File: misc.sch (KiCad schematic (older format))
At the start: 40 parts, among them J13 MICROSD_SLOT_TFP09-2-12B, P13 EXT_SD, P14 LCD, P15 LIMIT_SWITCHES, P16 LIMIT_SWITCHES_V, P17 CONN_01X03, P18 CONN_01X03, P19 CONN_01X03, P20 CONN_01X03, P21 THERMISTORS, P22 CONN_01X05, P25 CONN_01X03, SW1 RESET, U2 24LC256, U3 ESP-12E

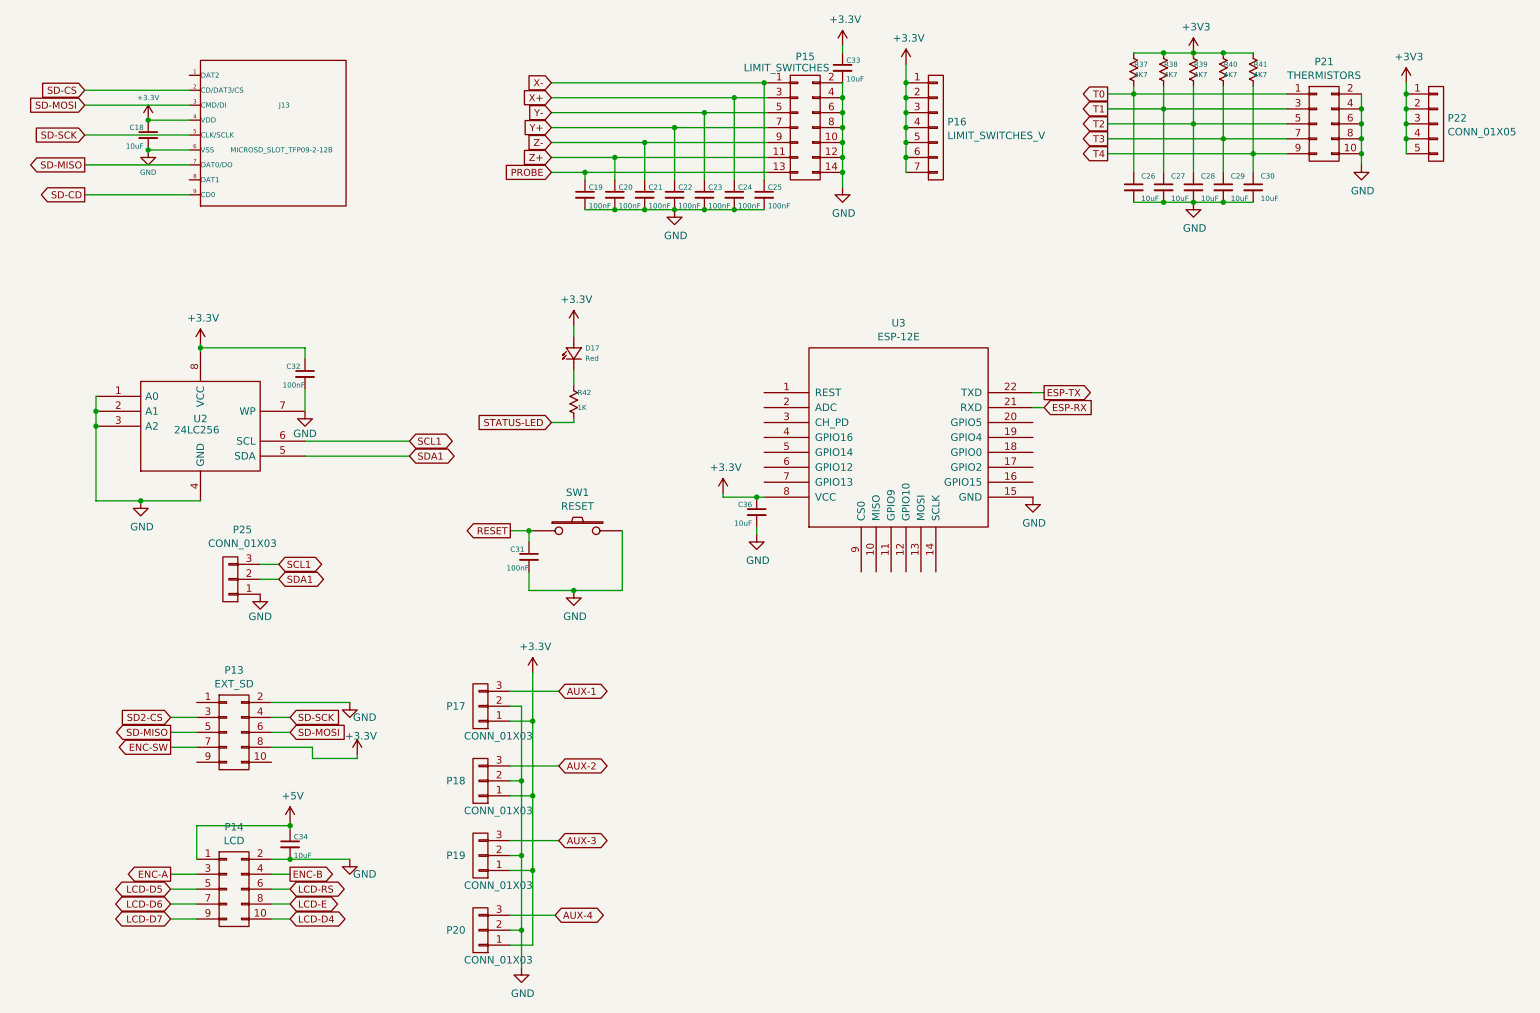
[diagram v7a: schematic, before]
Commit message: Added minimal arduino mega support
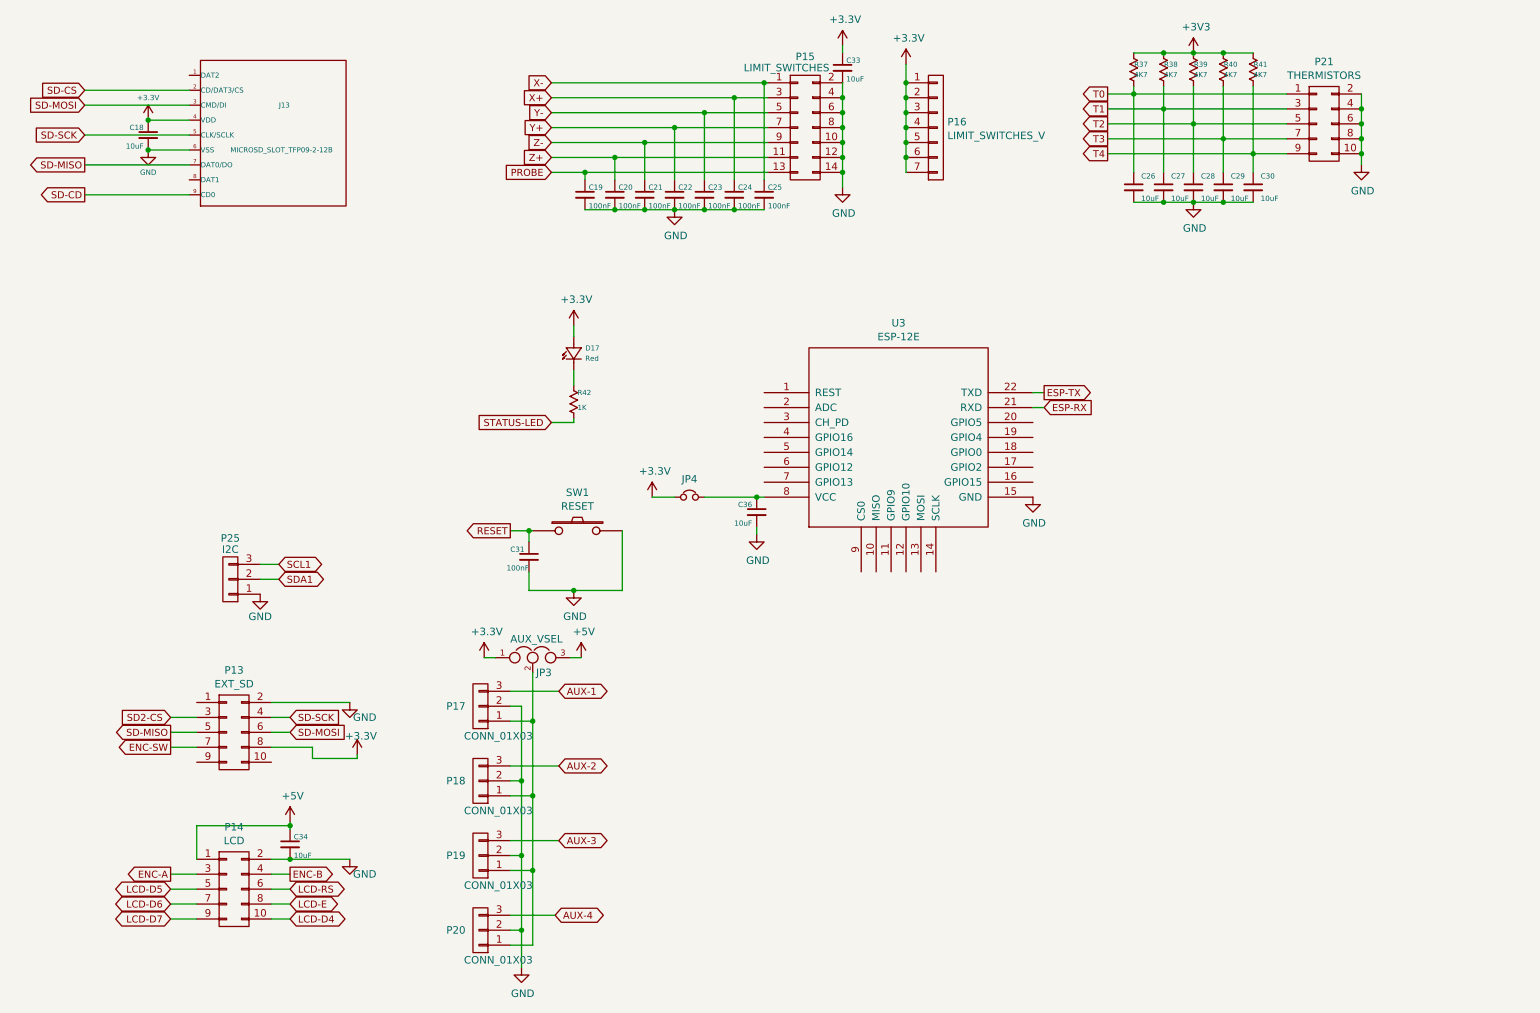
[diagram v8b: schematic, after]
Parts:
- removed C32: 100nF, capacitors:C_0603, symbol C_Small
- removed P22: CONN_01X05, headers:CON_HDR_1x5_2.54mm, symbol CONN_01X05
- removed U2: 24LC256, soic:SOIC8, symbol 24C16
- added JP3: AUX_VSEL, headers:CON_HDR_1x3_2.54mm, symbol JUMPER3
- added JP4: Jumper_NC_Small, headers:CON_HDR_1x2_2.54mm, symbol Jumper_NC_Small
- P25: value CONN_01X03 -> I2C
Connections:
- net +3V3: now also JP3.1, JP4.1; no longer C36.1, P17.1 (P1), P18.1 (P1), P19.1 (P1), P20.1 (P1), U3.8 (VCC)
- net +5V: now also JP3.3
- new net: JP3.2, P17.1 (P1), P18.1 (P1), P19.1 (P1), P20.1 (P1)
- new net: C36.1, JP4.2, U3.8 (VCC)
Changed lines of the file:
@@
 $EndComp
 $Comp
-L GND #PWR88
+L GND #PWR87
 U 1 1 568D834C
 P 9950 2075
-F 0 "#PWR88" H 9950 1825 50  0001 C CNN
+F 0 "#PWR87" H 9950 1825 50  0001 C CNN
 F 1 "GND" H 9958 1901 50  0000 C CNN
 F 2 "" H 9950 2075 50  0000 C CNN
@@
 $EndComp
 $Comp
-L GND #PWR87
+L GND #PWR86
 U 1 1 568D94E5
 P 8825 2325
-F 0 "#PWR87" H 8825 2075 50  0001 C CNN
+F 0 "#PWR86" H 8825 2075 50  0001 C CNN
 F 1 "GND" H 8833 2151 50  0000 C CNN
 F 2 "" H 8825 2325 50  0000 C CNN
@@
 $EndComp
 $Comp
-L +3V3 #PWR86
+L +3V3 #PWR85
 U 1 1 568D9512
 P 8825 1325
-F 0 "#PWR86" H 8825 1175 50  0001 C CNN
+F 0 "#PWR85" H 8825 1175 50  0001 C CNN
 F 1 "+3V3" H 8843 1499 50  0000 C CNN
 F 2 "" H 8825 1325 50  0000 C CNN
 F 3 "" H 8825 1325 50  0000 C CNN
 	1    8825 1325
-	1    0    0    -1
-$EndComp
-$Comp
-L CONN_01X05 P22
-U 1 1 568D989A
-P 10450 1800
-F 0 "P22" H 10527 1838 50  0000 L CNN
-F 1 "CONN_01X05" H 10527 1746 50  0000 L CNN
-F 2 "headers:CON_HDR_1x5_2.54mm" H 10450 1800 50  0001 C CNN
-F 3 "" H 10450 1800 50  0000 C CNN
-	1    10450 1800
-	1    0    0    -1
-$EndComp
-$Comp
-L +3V3 #PWR89
-U 1 1 568D9A56
-P 10250 1525
-F 0 "#PWR89" H 10250 1375 50  0001 C CNN
-F 1 "+3V3" H 10268 1699 50  0000 C CNN
-F 2 "" H 10250 1525 50  0000 C CNN
-F 3 "" H 10250 1525 50  0000 C CNN
-	1    10250 1525
-	1    0    0    -1
-$EndComp
-$Comp
-L 24C16 U2
-U 1 1 568DA07F
-P 2175 3825
-F 0 "U2" H 2175 3875 50  0000 C CNN
-F 1 "24LC256" H 2150 3800 50  0000 C CNN
-F 2 "soic:SOIC8" H 2175 3825 50  0001 C CNN
-F 3 "" H 2175 3825 50  0000 C CNN
-	1    2175 3825
-	1    0    0    -1
-$EndComp
-$Comp
-L GND #PWR71
-U 1 1 568DA443
-P 2875 3725
-F 0 "#PWR71" H 2875 3475 50  0001 C CNN
-F 1 "GND" H 2875 3575 50  0000 C CNN
-F 2 "" H 2875 3725 50  0000 C CNN
-F 3 "" H 2875 3725 50  0000 C CNN
-	1    2875 3725
-	1    0    0    -1
-$EndComp
-$Comp
-L GND #PWR65
-U 1 1 568DA52A
-P 1775 4325
-F 0 "#PWR65" H 1775 4075 50  0001 C CNN
-F 1 "GND" H 1783 4151 50  0000 C CNN
-F 2 "" H 1775 4325 50  0000 C CNN
-F 3 "" H 1775 4325 50  0000 C CNN
-	1    1775 4325
-	1    0    0    -1
-$EndComp
-$Comp
-L +3.3V #PWR68
-U 1 1 568DA65A
-P 2175 3275
-F 0 "#PWR68" H 2175 3125 50  0001 C CNN
-F 1 "+3.3V" H 2193 3449 50  0000 C CNN
-F 2 "" H 2175 3275 50  0000 C CNN
-F 3 "" H 2175 3275 50  0000 C CNN
-	1    2175 3275
 	1    0    0    -1
 $EndComp
@@
 $EndComp
 $Comp
-L GND #PWR83
+L GND #PWR82
 U 1 1 568D90A7
 P 6475 2225
-F 0 "#PWR83" H 6475 1975 50  0001 C CNN
+F 0 "#PWR82" H 6475 1975 50  0001 C CNN
 F 1 "GND" H 6483 2051 50  0000 C CNN
 F 2 "" H 6475 2225 50  0000 C CNN
@@
 $EndComp
 $Comp
-L +3.3V #PWR84
+L +3.3V #PWR83
 U 1 1 568D9133
 P 6900 1400
-F 0 "#PWR84" H 6900 1250 50  0001 C CNN
+F 0 "#PWR83" H 6900 1250 50  0001 C CNN
 F 1 "+3.3V" H 6918 1574 50  0000 C CNN
 F 2 "" H 6900 1400 50  0000 C CNN
@@
 	1    0    0    -1
 $EndComp
-Text GLabel 3575 3925 2    47   BiDi ~ 0
-SCL1
-Text GLabel 3575 4025 2    47   BiDi ~ 0
-SDA1
 $Comp
 L CONN_01X03 P20
@@
 	8250 2000 9450 2000
 Connection ~ 9225 2000
-Wire Wire Line
-	10250 1525 10250 2000
-Connection ~ 10250 1600
-Connection ~ 10250 1700
-Connection ~ 10250 1800
-Connection ~ 10250 1900
-Wire Wire Line
-	1475 3625 1475 4325
-Wire Wire Line
-	1475 4325 2175 4325
-Connection ~ 1475 3725
-Connection ~ 1475 3825
-Connection ~ 1775 4325
-Wire Wire Line
-	2175 3275 2175 3325
 Wire Wire Line
 	6900 1400 6900 2125
@@
 Connection ~ 5550 2375
 Connection ~ 5750 2375
-Wire Wire Line
-	2875 3925 3575 3925
-Wire Wire Line
-	2875 4025 3575 4025
 $Comp
 L CONN_01X03 P19
@@
 	4325 7200 4250 7200
 $Comp
-L GND #PWR75
+L GND #PWR74
 U 1 1 568EABC9
 P 4325 7450
-F 0 "#PWR75" H 4325 7200 50  0001 C CNN
+F 0 "#PWR74" H 4325 7200 50  0001 C CNN
 F 1 "GND" H 4333 7276 50  0000 C CNN
 F 2 "" H 4325 7450 50  0000 C CNN
@@
 $EndComp
 $Comp
-L +3.3V #PWR76
+L +3.3V #PWR73
 U 1 1 568EAEBC
-P 4400 5475
-F 0 "#PWR76" H 4400 5325 50  0001 C CNN
-F 1 "+3.3V" H 4418 5649 50  0000 C CNN
-F 2 "" H 4400 5475 50  0000 C CNN
-F 3 "" H 4400 5475 50  0000 C CNN
-	1    4400 5475
+P 4075 5375
+F 0 "#PWR73" H 4075 5225 50  0001 C CNN
+F 1 "+3.3V" H 4093 5549 50  0000 C CNN
+F 2 "" H 4075 5375 50  0000 C CNN
+F 3 "" H 4075 5375 50  0000 C CNN
+	1    4075 5375
 	1    0    0    -1
 $EndComp
@@
 SD-SCK
 $Comp
-L GND #PWR72
+L GND #PWR70
 U 1 1 568F027E
 P 3175 5675
-F 0 "#PWR72" H 3175 5425 50  0001 C CNN
+F 0 "#PWR70" H 3175 5425 50  0001 C CNN
 F 1 "GND" H 3275 5575 50  0000 C CNN
 F 2 "" H 3175 5675 50  0000 C CNN
@@
 	2650 5675 3175 5675
 $Comp
-L +3.3V #PWR74
+L +3.3V #PWR72
 U 1 1 568F1103
 P 3225 6025
-F 0 "#PWR74" H 3225 5875 50  0001 C CNN
+F 0 "#PWR72" H 3225 5875 50  0001 C CNN
 F 1 "+3.3V" H 3250 6150 50  0000 C CNN
 F 2 "" H 3225 6025 50  0000 C CNN
@@
 	3225 6050 3225 6025
 $Comp
-L +5V #PWR70
+L +5V #PWR69
 U 1 1 568F17B3
 P 2775 6475
-F 0 "#PWR70" H 2775 6325 50  0001 C CNN
+F 0 "#PWR69" H 2775 6325 50  0001 C CNN
 F 1 "+5V" H 2793 6649 50  0000 C CNN
 F 2 "" H 2775 6475 50  0000 C CNN
@@
 $EndComp
 $Comp
-L GND #PWR73
+L GND #PWR71
 U 1 1 568F18BA
 P 3175 6725
-F 0 "#PWR73" H 3175 6475 50  0001 C CNN
+F 0 "#PWR71" H 3175 6475 50  0001 C CNN
 F 1 "GND" H 3275 6625 50  0000 C CNN
 F 2 "" H 3175 6725 50  0000 C CNN
@@
 	4675 3800 4675 3775
 $Comp
-L +3.3V #PWR77
+L +3.3V #PWR75
 U 1 1 568F9643
 P 4675 3150
-F 0 "#PWR77" H 4675 3000 50  0001 C CNN
+F 0 "#PWR75" H 4675 3000 50  0001 C CNN
 F 1 "+3.3V" H 4693 3324 50  0000 C CNN
 F 2 "" H 4675 3150 50  0000 C CNN
@@
 	4250 4525 4400 4525
 $Comp
-L GND #PWR78
+L GND #PWR76
 U 1 1 568F9E88
 P 4675 4925
-F 0 "#PWR78" H 4675 4675 50  0001 C CNN
+F 0 "#PWR76" H 4675 4675 50  0001 C CNN
 F 1 "GND" H 4683 4751 50  0000 C CNN
 F 2 "" H 4675 4925 50  0000 C CNN
@@
 Wire Wire Line
 	5000 4925 5000 4525
-$Comp
-L C_Small C32
-U 1 1 568FAA2A
-P 2875 3475
-F 0 "C32" H 2750 3525 35  0000 L CNN
-F 1 "100nF" H 2725 3400 35  0000 L CNN
-F 2 "capacitors:C_0603" H 2875 3475 50  0001 C CNN
-F 3 "" H 2875 3475 50  0000 C CNN
-	1    2875 3475
-	1    0    0    -1
-$EndComp
-Wire Wire Line
-	2875 3575 2875 3725
-Wire Wire Line
-	2875 3300 2875 3375
-Wire Wire Line
-	2875 3300 2175 3300
-Connection ~ 2175 3300
 Connection ~ 4400 5800
 Connection ~ 4325 7200
@@
 $EndComp
 $Comp
-L +3.3V #PWR82
+L +3.3V #PWR81
 U 1 1 56944144
 P 6475 1275
-F 0 "#PWR82" H 6475 1125 50  0001 C CNN
+F 0 "#PWR81" H 6475 1125 50  0001 C CNN
 F 1 "+3.3V" H 6493 1449 50  0000 C CNN
 F 2 "" H 6475 1275 50  0000 C CNN
@@
 $EndComp
 $Comp
-L +3.3V #PWR80
+L +3.3V #PWR78
 U 1 1 56BB7176
-P 5675 4275
-F 0 "#PWR80" H 5675 4125 50  0001 C CNN
-F 1 "+3.3V" H 5693 4449 50  0000 C CNN
-F 2 "" H 5675 4275 50  0000 C CNN
-F 3 "" H 5675 4275 50  0000 C CNN
-	1    5675 4275
-	1    0    0    -1
-$EndComp
-Wire Wire Line
-	5950 4300 5675 4300
-Wire Wire Line
-	5675 4300 5675 4275
-$Comp
-L GND #PWR85
+P 5200 4300
+F 0 "#PWR78" H 5200 4150 50  0001 C CNN
+F 1 "+3.3V" H 5218 4474 50  0000 C CNN
+F 2 "" H 5200 4300 50  0000 C CNN
+F 3 "" H 5200 4300 50  0000 C CNN
+	1    5200 4300
+	1    0    0    -1
+$EndComp
+Wire Wire Line
+	5550 4300 5950 4300
+$Comp
+L GND #PWR84
 U 1 1 56BB74F0
 P 7750 4300
-F 0 "#PWR85" H 7750 4050 50  0001 C CNN
+F 0 "#PWR84" H 7750 4050 50  0001 C CNN
 F 1 "GND" H 7758 4126 50  0000 C CNN
 F 2 "" H 7750 4300 50  0000 C CNN
@@
 U 1 1 56C3648D
 P 2375 4850
-F 0 "P25" H 2294 4518 50  0000 C CNN
-F 1 "CONN_01X03" H 2294 4610 50  0000 C CNN
+F 0 "P25" H 2375 4575 50  0000 C CNN
+F 1 "I2C" H 2375 4650 50  0000 C CNN
 F 2 "headers:CON_HDR_1x3_2.54mm" H 2375 4850 50  0001 C CNN
 F 3 "" H 2375 4850 50  0000 C CNN
@@
 	2700 4850 2575 4850
 $Comp
-L GND #PWR69
+L GND #PWR68
 U 1 1 56C36C49
 P 2575 4950
-F 0 "#PWR69" H 2575 4700 50  0001 C CNN
+F 0 "#PWR68" H 2575 4700 50  0001 C CNN
 F 1 "GND" H 2575 4800 50  0000 C CNN
 F 2 "" H 2575 4950 50  0000 C CNN
@@
 $EndComp
 $Comp
-L GND #PWR81
+L GND #PWR80
 U 1 1 56C38FAF
 P 5900 4550
-F 0 "#PWR81" H 5900 4300 50  0001 C CNN
+F 0 "#PWR80" H 5900 4300 50  0001 C CNN
 F 1 "GND" H 5908 4376 50  0000 C CNN
 F 2 "" H 5900 4550 50  0000 C CNN
@@
 Wire Wire Line
 	5900 4550 5900 4500
+$Comp
+L JUMPER3 JP3
+U 1 1 56C468CA
+P 4400 5375
+F 0 "JP3" H 4475 5275 50  0000 C CNN
+F 1 "AUX_VSEL" H 4425 5500 50  0000 C CNN
+F 2 "headers:CON_HDR_1x3_2.54mm" H 4400 5375 50  0001 C CNN
+F 3 "" H 4400 5375 50  0000 C CNN
+	1    4400 5375
+	1    0    0    -1
+$EndComp
+$Comp
+L +5V #PWR77
+U 1 1 56C47004
+P 4725 5375
+F 0 "#PWR77" H 4725 5225 50  0001 C CNN
+F 1 "+5V" H 4743 5549 50  0000 C CNN
+F 2 "" H 4725 5375 50  0000 C CNN
+F 3 "" H 4725 5375 50  0000 C CNN
+	1    4725 5375
+	1    0    0    -1
+$EndComp
+Wire Wire Line
+	4075 5375 4150 5375
+Wire Wire Line
+	4650 5375 4725 5375
+$Comp
+L Jumper_NC_Small JP4
+U 1 1 56C5EDDD
+P 5450 4300
+F 0 "JP4" H 5450 4421 50  0000 C CNN
+F 1 "Jumper_NC_Small" H 5460 4240 50  0001 C CNN
+F 2 "headers:CON_HDR_1x2_2.54mm" H 5450 4421 50  0001 C CNN
+F 3 "" H 5450 4300 50  0000 C CNN
+	1    5450 4300
+	1    0    0    -1
+$EndComp
+Wire Wire Line
+	5350 4300 5200 4300
 $EndSCHEMATC
